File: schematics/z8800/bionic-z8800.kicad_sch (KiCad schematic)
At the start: 8 parts, among them J1 Bionic-P135, J2 Bionic-P245, U1 Z88C00, U2 11AA010-I/TT

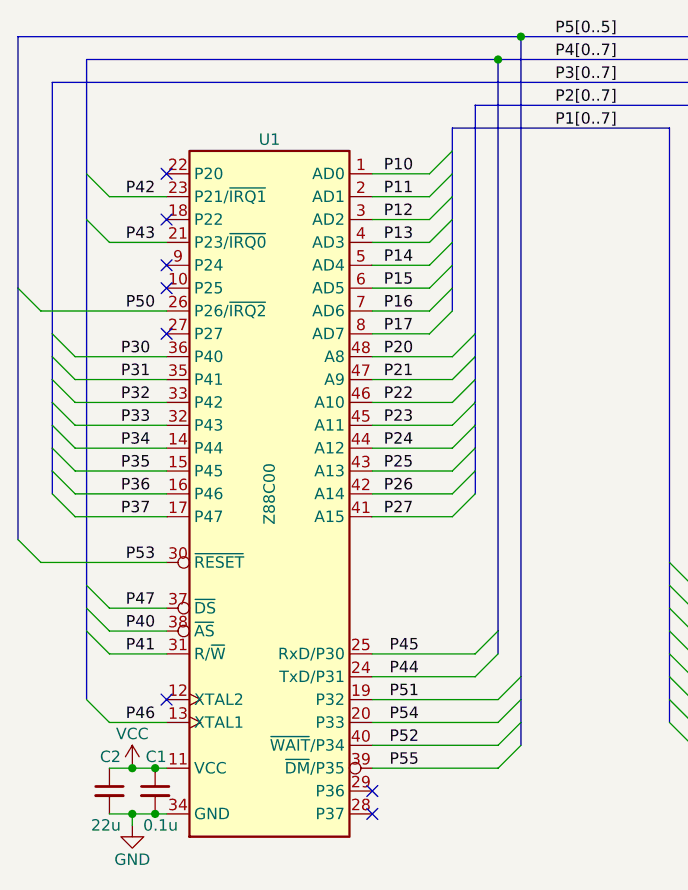
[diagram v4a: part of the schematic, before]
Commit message: [Z8800] Fix Z8800 symbol
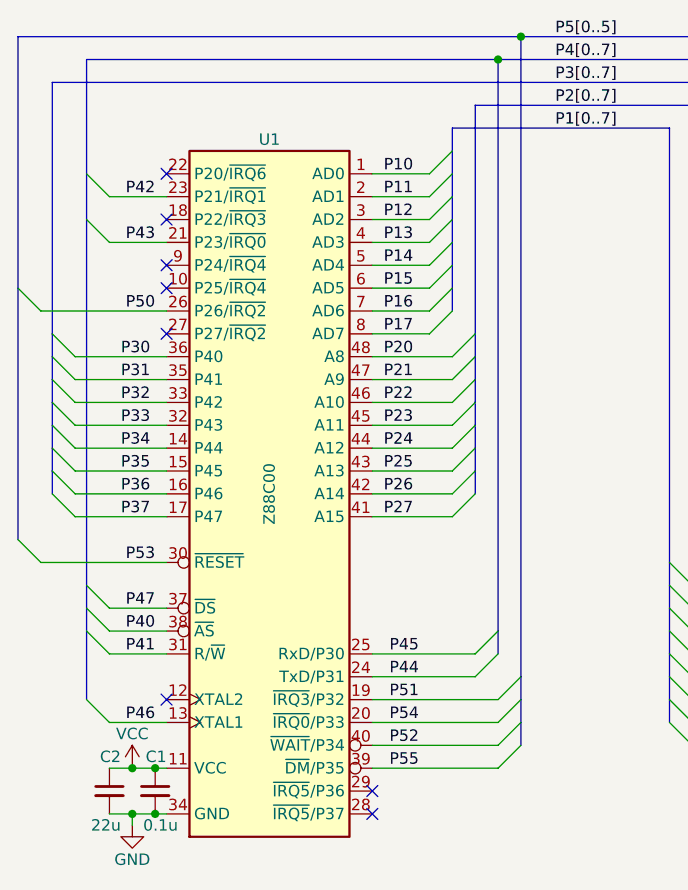
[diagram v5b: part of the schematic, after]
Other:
- title: BionicZ8800 -> BionicZ88C00
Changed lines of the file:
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@@
 	(paper "A4")
 	(title_block
-		(title "BionicZ8800")
-		(date "2024-11-02")
+		(title "BionicZ88C00")
+		(date "2024-12-19")
 		(rev "5")
 		(company "Tadashi G. Takaoka")

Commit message: [Z8800] Cleanup schematics
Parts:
- D1: footprint 0-LocalLibrary:LED_CSL1901UW1_ROM-M -> rhom:LED_CSL1901UW1_ROM-M; symbol 0-LocalLibrary:CSL1901UW1 -> rhom:CSL1901UW1
- J1: footprint 0-LocalLibrary:Bionic-P135_Vertical -> bionic:Bionic-P135_Vertical; symbol 0-LocalLibrary:Bionic-P135 -> bionic:Bionic-P135
- J2: footprint 0-LocalLibrary:Bionic-P245_Vertical -> bionic:Bionic-P245_Vertical; symbol 0-LocalLibrary:Bionic-P245 -> bionic:Bionic-P245
- U1: footprint 0-LocalLibrary:DIP-48_W15.24mm_Socket -> bionic:DIP-48_W15.24mm_Socket; symbol 0-LocalLibrary:Z88C00 -> cpu:Z88C00
- U2: footprint 0-LocalLibrary:SOT-23_MC_MCH-M -> microchip:SOT-23_MC_MCH-M; symbol 0-LocalLibrary:11AA010-I_TT -> microchip:11AA010-I_TT
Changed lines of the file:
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@@
 	)
 	(symbol
-		(lib_id "0-LocalLibrary:Z88C00")
+		(lib_id "cpu:Z88C00")
 		(at 93.98 99.06 0)
 		(unit 1)
@@
 			)
 		)
-		(property "Footprint" "0-LocalLibrary:DIP-48_W15.24mm_Socket"
-			(at 93.98 140.97 0)
+		(property "Footprint" "bionic:DIP-48_W15.24mm_Socket"
+			(at 93.472 146.558 0)
 			(effects
 				(font
@@
 		)
 		(property "Datasheet" "https://datasheetspdf.com/pdf-file/527631/Zilog/Z88C00/1"
-			(at 93.98 91.44 0)
-			(effects
-				(font
-					(size 1.27 1.27)
-				)
-				(hide yes)
-			)
-		)
-		(property "Description" ""
-			(at 93.98 99.06 0)
+			(at 93.726 143.51 0)
+			(effects
+				(font
+					(size 1.27 1.27)
+				)
+				(hide yes)
+			)
+		)
+		(property "Description" "8-bit General Purpose Microprocessor, DIP-40"
+			(at 93.726 140.208 0)
 			(effects
 				(font
@@
 	)
 	(symbol
-		(lib_id "0-LocalLibrary:CSL1901UW1")
+		(lib_id "rhom:CSL1901UW1")
 		(at 201.93 33.02 270)
 		(unit 1)
@@
 		(fields_autoplaced yes)
 		(property "Reference" "D1"
-			(at 205.74 35.433 90)
+			(at 205.74 35.4329 90)
 			(effects
 				(font
@@
 		)
 		(property "Value" "CSL1901UW1"
-			(at 205.74 37.973 90)
+			(at 205.74 37.9729 90)
 			(effects
 				(font
@@
 			)
 		)
-		(property "Footprint" "0-LocalLibrary:LED_CSL1901UW1_ROM-M"
+		(property "Footprint" "rhom:LED_CSL1901UW1_ROM-M"
 			(at 193.04 36.83 0)
 			(effects
@@
 	)
 	(symbol
-		(lib_id "0-LocalLibrary:11AA010-I_TT")
+		(lib_id "microchip:11AA010-I_TT")
 		(at 190.5 72.39 0)
 		(unit 1)
@@
 			)
 		)
-		(property "Footprint" "0-LocalLibrary:SOT-23_MC_MCH-M"
+		(property "Footprint" "microchip:SOT-23_MC_MCH-M"
 			(at 193.04 90.17 0)
 			(effects
@@
 			)
 		)
-		(property "Description" ""
+		(property "Description" "UNI/O Serial EEPROM (1Kbit)"
 			(at 190.5 72.39 0)
 			(effects
@@
 	)
 	(symbol
-		(lib_id "0-LocalLibrary:Bionic-P245")
+		(lib_id "bionic:Bionic-P245")
 		(at 165.1 99.06 0)
 		(unit 1)
@@
 			)
 		)
-		(property "Footprint" "0-LocalLibrary:Bionic-P245_Vertical"
+		(property "Footprint" "bionic:Bionic-P245_Vertical"
 			(at 166.37 134.62 0)
 			(effects
@@
 			)
 		)
-		(property "Description" ""
+		(property "Description" "Generic connector, single row, 01x24, script generated (kicad-library-utils/schlib/autogen/connector/)"
 			(at 165.1 99.06 0)
 			(effects
@@
 	)
 	(symbol
-		(lib_id "0-LocalLibrary:Bionic-P135")
+		(lib_id "bionic:Bionic-P135")
 		(at 157.48 99.06 0)
 		(unit 1)
@@
 			)
 		)
-		(property "Footprint" "0-LocalLibrary:Bionic-P135_Vertical"
+		(property "Footprint" "bionic:Bionic-P135_Vertical"
 			(at 158.75 134.62 0)
 			(effects
@@
 			)
 		)
-		(property "Description" ""
+		(property "Description" "Generic connector, single row, 01x24, script generated (kicad-library-utils/schlib/autogen/connector/)"
 			(at 157.48 99.06 0)
 			(effects

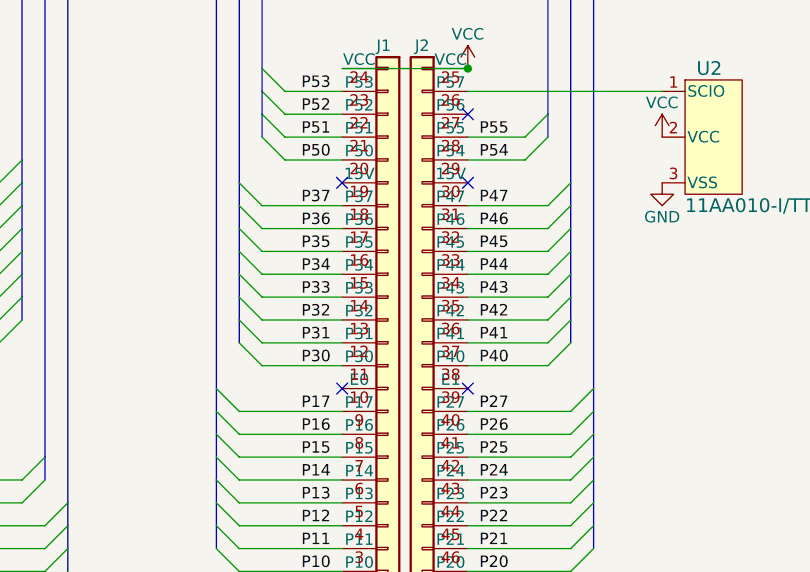
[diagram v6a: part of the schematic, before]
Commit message: [Z8800] Update schematics
Remove unused pins from bionic connector
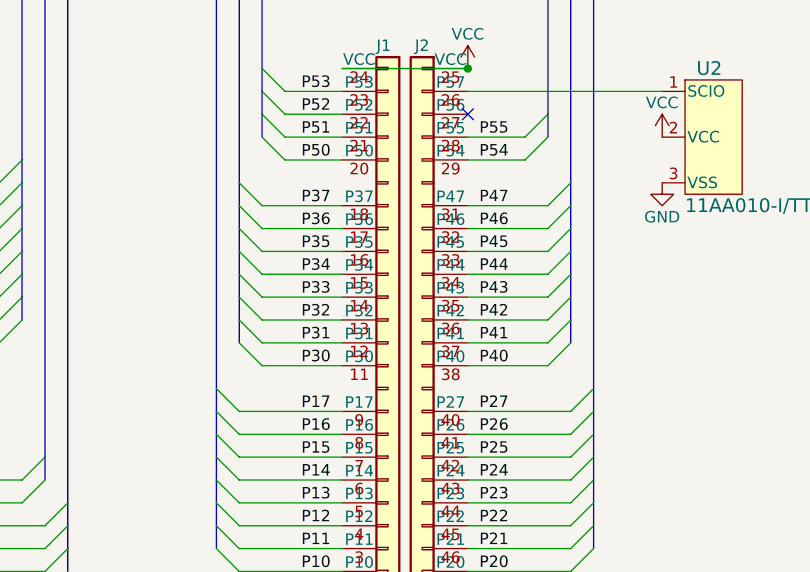
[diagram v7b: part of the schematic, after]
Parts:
- J1: footprint bionic:Bionic-P135_Vertical -> bionic:Bionic-P135_THT
- J2: footprint bionic:Bionic-P245_Vertical -> bionic:Bionic-P245_THT
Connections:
- no-connect marks 13 -> 9
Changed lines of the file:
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@@
 	(title_block
 		(title "BionicZ88C00")
-		(date "2024-12-19")
-		(rev "5")
+		(date "2025-03-02")
+		(rev "6")
 		(company "Tadashi G. Takaoka")
 	)
@@
 	)
 	(no_connect
-		(at 152.4 83.82)
-	)
-	(no_connect
 		(at 82.55 121.92)
 	)
@@
 	)
 	(no_connect
-		(at 152.4 106.68)
-	)
-	(no_connect
 		(at 82.55 81.28)
 	)
@@
 	)
 	(no_connect
-		(at 166.37 106.68)
-	)
-	(no_connect
 		(at 166.37 76.2)
 	)
 	(no_connect
-		(at 166.37 83.82)
-	)
-	(no_connect
 		(at 82.55 68.58)
 	)
@@
 			)
 		)
-		(property "Footprint" "bionic:Bionic-P245_Vertical"
+		(property "Footprint" "bionic:Bionic-P245_THT"
 			(at 166.37 134.62 0)
 			(effects
@@
 		(pin "48"
 		)
-		(pin "39"
-		)
 		(pin "40"
 		)
@@
 		(pin "33"
 		)
-		(pin "30"
-		)
 		(pin "25"
 		)
@@
 			)
 		)
-		(property "Footprint" "bionic:Bionic-P135_Vertical"
+		(property "Footprint" "bionic:Bionic-P135_THT"
 			(at 158.75 134.62 0)
 			(effects
@@
 		(pin "2"
 		)
-		(pin "19"
-		)
 		(pin "18"
 		)
@@
 		(pin "3"
 		)
-		(pin "10"
-		)
 		(pin "9"
